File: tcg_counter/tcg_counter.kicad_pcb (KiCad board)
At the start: 2 copper layers, 63 x 88 mm, 23 parts, among them P1 TC2050-IDC-430, U1 TCAL9539RTW, U3 RF430FRL152

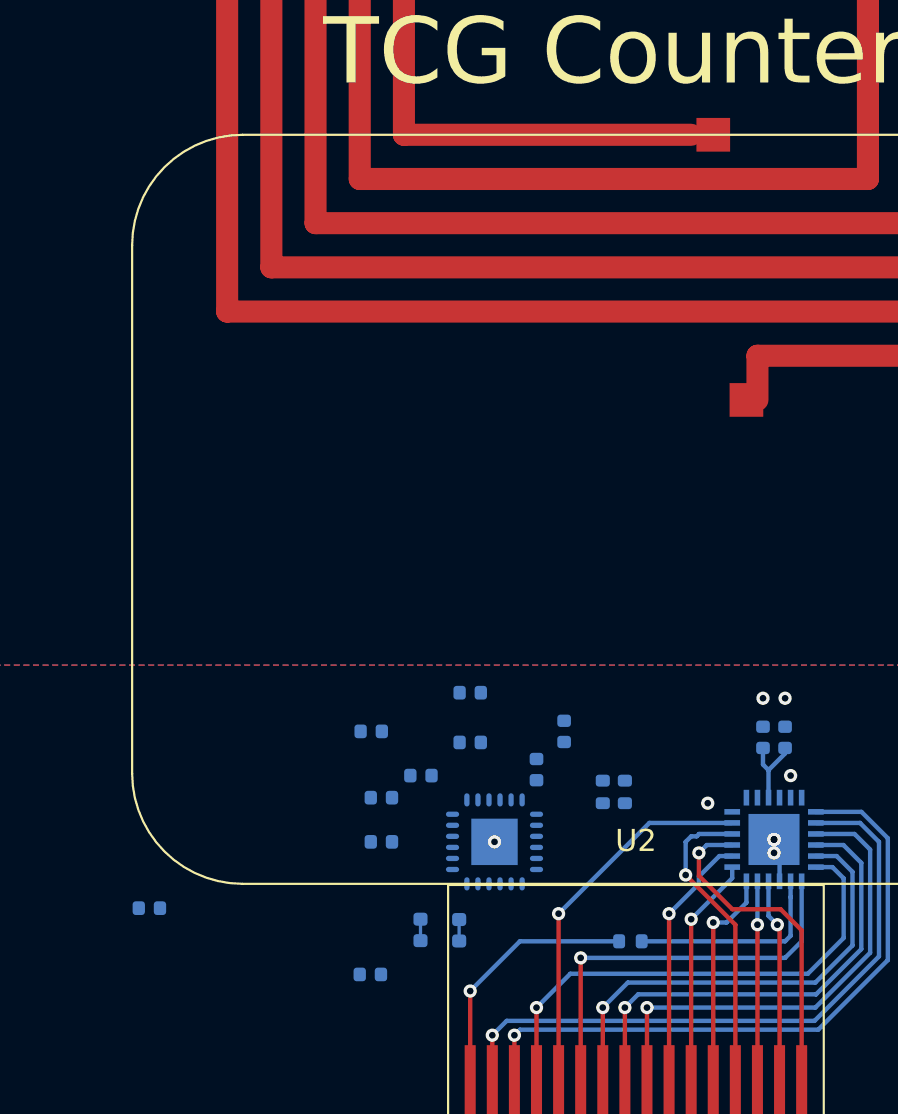
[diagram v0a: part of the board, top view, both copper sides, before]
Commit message: Routing to antenna and some capacitors
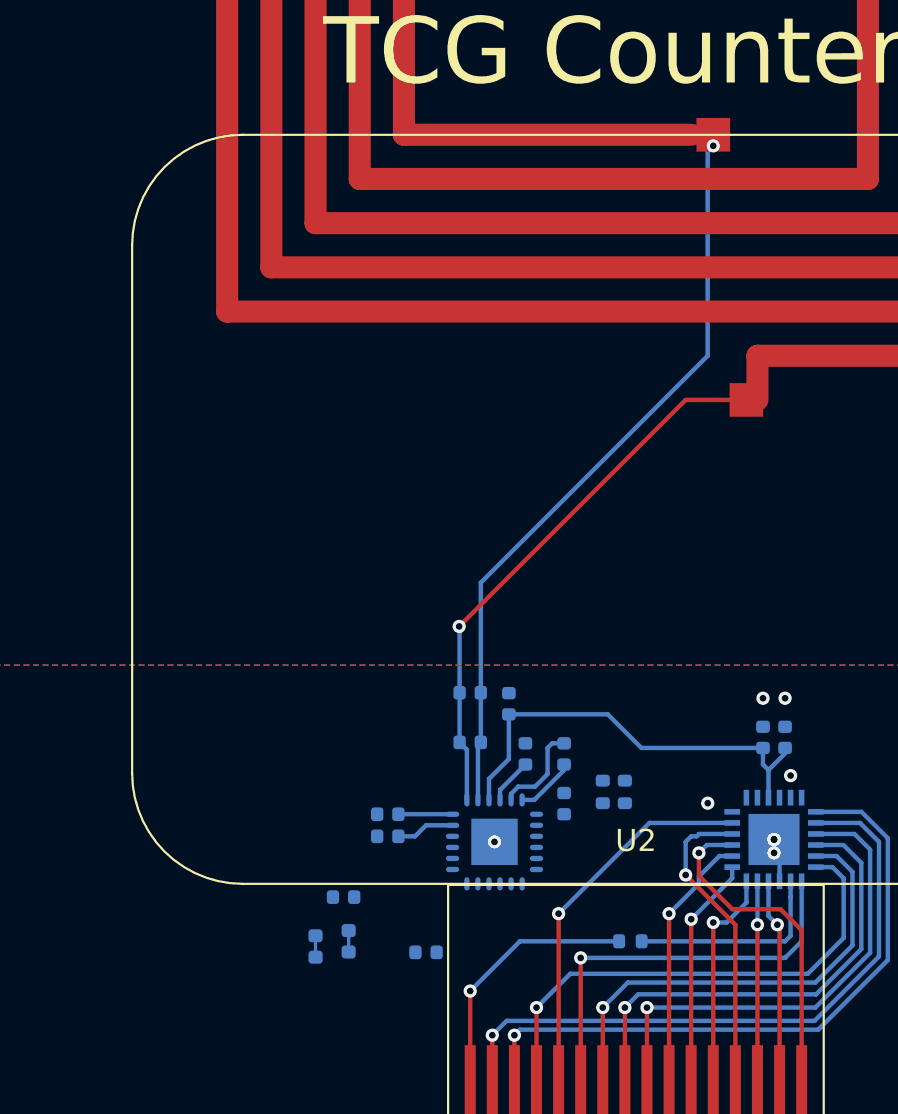
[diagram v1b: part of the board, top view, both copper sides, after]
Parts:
- moved C9 8.80 mm to (128.3, 106.5)
- moved C1 7.05 mm to (136.5, 100.0), turned to 90 degrees
- moved C2 5.14 mm to (135.8, 97.8), turned to 90 degrees
- moved R3 5.02 mm to (128.5, 108.5)
- moved R2 4.81 mm to (127.0, 108.7)
- moved C5 3.27 mm to (138.2, 102.3)
- moved C6 2.71 mm to (132.0, 109.0)
- moved C7 1.44 mm to (138.2, 100.0)
- moved C3 0.80 mm to (130.3, 102.8)
- moved C4 0.38 mm to (130.3, 103.8)
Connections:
- C1 pad 1: Net-(U3-VDDB) -> VDDB
- P1 pad 2: unconnected-(P1-VCC_Tool-Pad2) -> VDDSW
- P1 pad 6: unconnected-(P1-NC-Pad6) -> VDDB
- U1 pad 25: GND -> (no net)
- U3 pad 4: Net-(U3-VDDB) -> VDDB
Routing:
- net Net-(U3-ANT2): track 0.00 -> 34.5 mm, vias 0 -> 1
- net Net-(U3-ANT1): track 0.00 -> 24.9 mm, vias 0 -> 1
- net VDDSW: track 3.66 -> 19.8 mm
- net Net-(U3-CP1): track 0.00 -> 4.31 mm
- net Net-(U3-CP2): track 0.00 -> 2.71 mm
- net Net-(U3-VDDH): track 0.00 -> 2.66 mm
- net Net-(U3-VDDD): track 0.00 -> 2.45 mm
- net VDDB: track 0.00 -> 2.08 mm

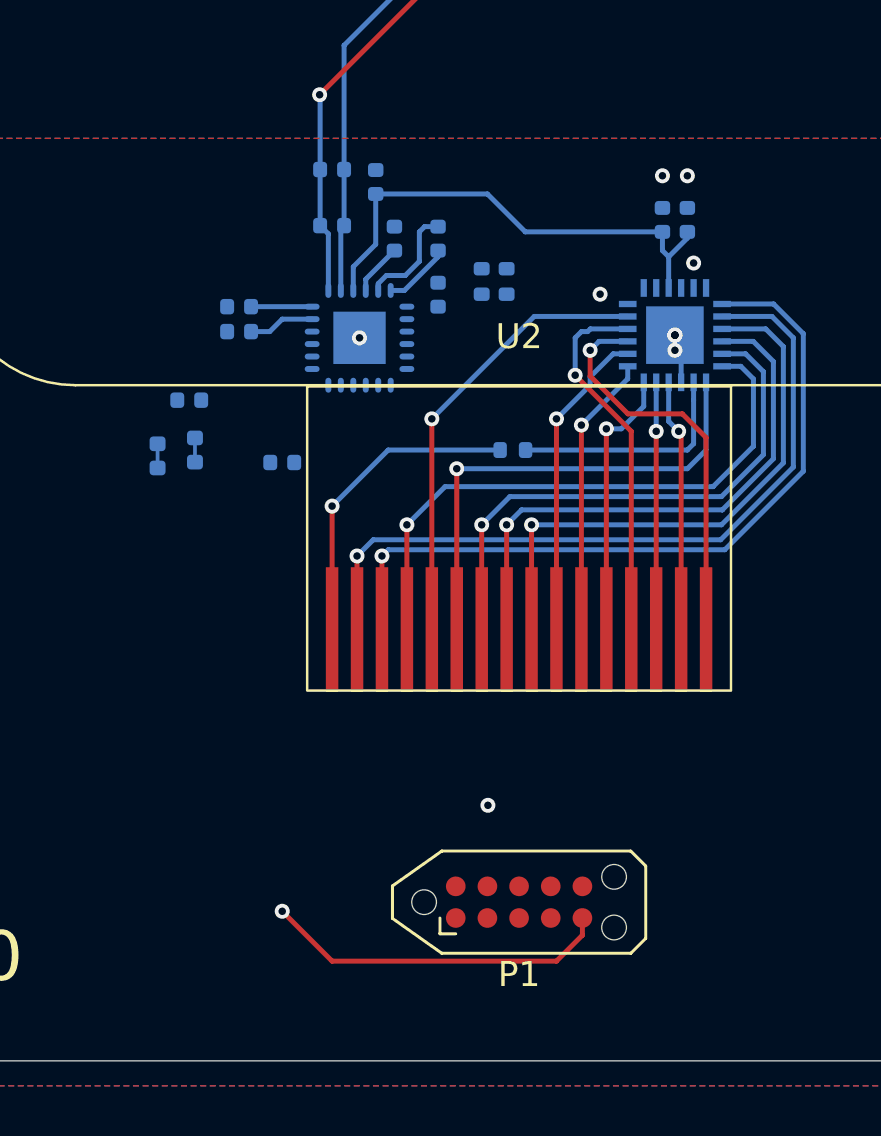
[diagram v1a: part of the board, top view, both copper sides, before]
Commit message: Finished traces, made new footprint for TCAL9539
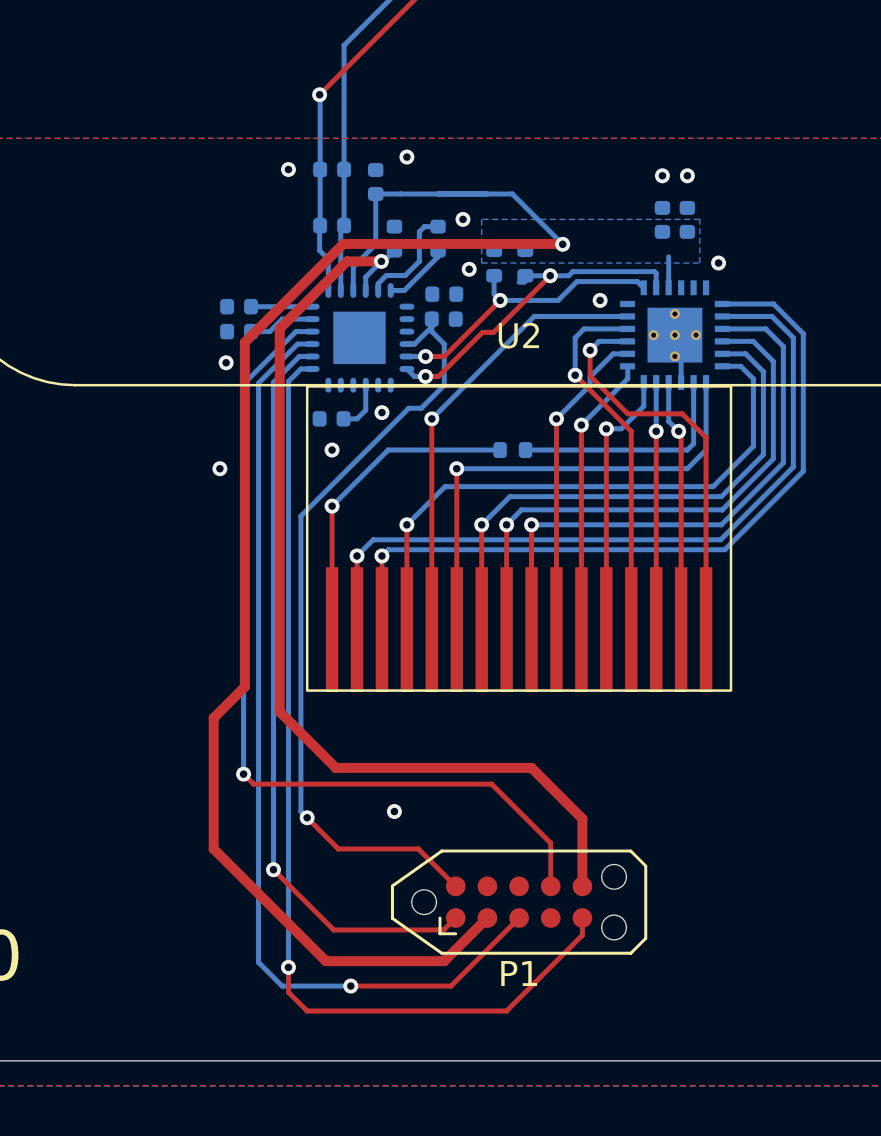
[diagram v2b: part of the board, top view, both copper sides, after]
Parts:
- removed R2, R3: DNP, footprints:R_0402_shorted
- U1: footprint tcal:WQFN24_RTW-J_TEX-L -> TIFootprints:TI_RTW24_4x4mm_EP2.2mm
- moved C6 8.66 mm to (138.5, 103.2), turned to 0 degrees
- moved C9 5.76 mm to (134.0, 107.2), turned to 0 degrees
- moved R5 1.05 mm to (141.8, 101.0)
- moved R4 0.89 mm to (140.5, 101.0)
- moved C5 0.25 mm to (138.5, 102.2), turned to 0 degrees
- turned U1 to -90 degrees
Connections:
- U1 pad 25: (no net) -> GND
- U3 pad 14: Net-(U3-TST2) -> GND
- U3 pad 16: Net-(U3-TST1) -> GND
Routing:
- net VDDSW: track 19.8 -> 64.4 mm, vias 0 -> 1
- net TDI: track 0.00 -> 38.0 mm, vias 0 -> 1
- net VDDB: track 2.08 -> 39.3 mm, vias 0 -> 1
- net TCK: track 0.00 -> 34.5 mm, vias 0 -> 1
- net Net-(P1-~{RST}): track 0.00 -> 31.7 mm, vias 0 -> 1
- net TDO: track 0.00 -> 30.0 mm, vias 0 -> 1
- net TMS: track 14.0 -> 39.7 mm
- net /P1.0: track 0.00 -> 13.7 mm, vias 0 -> 2
- net /P1.1: track 0.00 -> 11.9 mm, vias 0 -> 2
- net /SVSS: track 0.00 -> 2.03 mm
- net GND: vias 9 -> 13
- added copper zone on B.Cu, net VDDSW
